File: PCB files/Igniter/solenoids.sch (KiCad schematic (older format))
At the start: 29 parts, among them Q2 N MOSFET, Q4 N MOSFET, U2 FDS8984, U3 FDS8984, U4 FDS8984

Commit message: 12/5/2019
-Updated netlist and board layout with added dsub15 for solenoids
-Fixed all barrel jack connectors
-Removed some 2560 pins for routing
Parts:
- J4: renamed from J?; footprint (none) -> Connector_Dsub:DSUB-15-HD_Female_Horizontal_P2.29x1.98mm_EdgePinOffset3.03mm_Housed_MountingHolesOffset4.94mm
- gave numbers to parts that had none: 9
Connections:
- wire segments 77 -> 78
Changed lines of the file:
@@
 LIBS:interface
 LIBS:Igniter-cache
-EELAYER 29 0
+EELAYER 26 0
 EELAYER END
 $Descr A4 11693 8268
@@
 Connection ~ 8225 3660
 $Comp
-L Connector:Conn_01x11_Female J?
+L Connector:Conn_01x11_Female J4
 U 1 1 5DE8A6FF
 P 6176 2383
-F 0 "J?" V 6341 2363 50  0000 C CNN
+F 0 "J4" V 6341 2363 50  0000 C CNN
 F 1 "SOL_D15" V 6250 2363 50  0000 C CNN
-F 2 "" H 6176 2383 50  0001 C CNN
+F 2 "Connector_Dsub:DSUB-15-HD_Female_Horizontal_P2.29x1.98mm_EdgePinOffset3.03mm_Housed_MountingHolesOffset4.94mm" H 6176 2383 50  0001 C CNN
 F 3 "~" H 6176 2383 50  0001 C CNN
 	1    6176 2383
@@
 SOL1-
 $Comp
-L power:GNDREF #PWR?
+L power:GNDREF #PWR032
 U 1 1 5DF3EB19
 P 5922 2883
-F 0 "#PWR?" H 5922 2633 50  0001 C CNN
+F 0 "#PWR032" H 5922 2633 50  0001 C CNN
 F 1 "GNDREF" H 5927 2710 50  0001 C CNN
 F 2 "" H 5922 2883 50  0001 C CNN
@@
 	3784 2424 3684 2524
 Entry Wire Line
-	3941 4352 3841 4452
+	3783 4000 3683 4100
 Entry Wire Line
-	3957 4699 3857 4799
+	3783 4381 3683 4481
 Wire Wire Line
 	2927 2775 2927 2803
@@
 P 4783 3391
 AR Path="/5DFE00A1" Ref="#PWR?"  Part="1"
-AR Path="/5DB4D508/5DFE00A1" Ref="#PWR?"  Part="1"
-F 0 "#PWR?" H 4783 3141 50  0001 C CNN
+AR Path="/5DB4D508/5DFE00A1" Ref="#PWR030"  Part="1"
+F 0 "#PWR030" H 4783 3141 50  0001 C CNN
 F 1 "GNDREF" H 4788 3218 50  0001 C CNN
 F 2 "" H 4783 3391 50  0001 C CNN
@@
 P 4783 3241
 AR Path="/5DFE00AB" Ref="R?"  Part="1"
-AR Path="/5DB4D508/5DFE00AB" Ref="R?"  Part="1"
-F 0 "R?" V 4703 3191 50  0000 L CNN
+AR Path="/5DB4D508/5DFE00AB" Ref="R3"  Part="1"
+F 0 "R3" V 4703 3191 50  0000 L CNN
 F 1 "10k" V 4783 3171 50  0000 L CNN
 F 2 "Resistor_SMD:R_1206_3216Metric" V 4713 3241 50  0001 C CNN
@@
 $EndComp
 $Comp
-L power:+24V #PWR?
+L power:+24V #PWR019
 U 1 1 5DFE00B5
 P 4443 2307
-F 0 "#PWR?" H 4443 2157 50  0001 C CNN
+F 0 "#PWR019" H 4443 2157 50  0001 C CNN
 F 1 "+24V" H 4458 2480 50  0000 C CNN
 F 2 "" H 4443 2307 50  0001 C CNN
@@
 AR Path="/5D9BEB88/5DFE00C0" Ref="Q?"  Part="1"
 AR Path="/5DFE00C0" Ref="Q?"  Part="1"
-AR Path="/5DB4D508/5DFE00C0" Ref="Q?"  Part="1"
-F 0 "Q?" H 4749 3137 50  0000 L CNN
+AR Path="/5DB4D508/5DFE00C0" Ref="Q5"  Part="1"
+F 0 "Q5" H 4749 3137 50  0000 L CNN
 F 1 "N MOSFET" H 4749 3091 50  0001 L CNN
 F 2 "Package_TO_SOT_SMD:SOT-223" H 4743 3191 50  0001 C CNN
@@
 	4443 3291 4443 3391
 $Comp
-L power:GNDREF #PWR?
+L power:GNDREF #PWR020
 U 1 1 5DFE00CB
 P 4443 3391
-F 0 "#PWR?" H 4443 3141 50  0001 C CNN
+F 0 "#PWR020" H 4443 3141 50  0001 C CNN
 F 1 "GNDREF" H 4448 3218 50  0001 C CNN
 F 2 "" H 4443 3391 50  0001 C CNN
@@
 $EndComp
 $Comp
-L Device:D D?
+L Device:D D5
 U 1 1 5DFE00D5
 P 4443 2626
-F 0 "D?" V 4397 2705 50  0000 L CNN
+F 0 "D5" V 4397 2705 50  0000 L CNN
 F 1 "D" V 4488 2705 50  0000 L CNN
 F 2 "Diode_SMD:D_SOD-123F" H 4443 2626 50  0001 C CNN
@@
 P 2586 4968
 AR Path="/5DFFE41D" Ref="#PWR?"  Part="1"
-AR Path="/5DB4D508/5DFFE41D" Ref="#PWR?"  Part="1"
-F 0 "#PWR?" H 2586 4718 50  0001 C CNN
+AR Path="/5DB4D508/5DFFE41D" Ref="#PWR014"  Part="1"
+F 0 "#PWR014" H 2586 4718 50  0001 C CNN
 F 1 "GNDREF" H 2591 4795 50  0001 C CNN
 F 2 "" H 2586 4968 50  0001 C CNN
@@
 P 2586 4818
 AR Path="/5DFFE427" Ref="R?"  Part="1"
-AR Path="/5DB4D508/5DFFE427" Ref="R?"  Part="1"
-F 0 "R?" V 2506 4768 50  0000 L CNN
+AR Path="/5DB4D508/5DFFE427" Ref="R2"  Part="1"
+F 0 "R2" V 2506 4768 50  0000 L CNN
 F 1 "10k" V 2586 4748 50  0000 L CNN
 F 2 "Resistor_SMD:R_1206_3216Metric" V 2516 4818 50  0001 C CNN
@@
 $EndComp
 $Comp
-L power:+24V #PWR?
+L power:+24V #PWR015
 U 1 1 5DFFE431
 P 2926 3884
-F 0 "#PWR?" H 2926 3734 50  0001 C CNN
+F 0 "#PWR015" H 2926 3734 50  0001 C CNN
 F 1 "+24V" H 2941 4057 50  0000 C CNN
 F 2 "" H 2926 3884 50  0001 C CNN
@@
 AR Path="/5D9BEB88/5DFFE43C" Ref="Q?"  Part="1"
 AR Path="/5DFFE43C" Ref="Q?"  Part="1"
-AR Path="/5DB4D508/5DFFE43C" Ref="Q?"  Part="1"
-F 0 "Q?" H 3032 4714 50  0000 L CNN
+AR Path="/5DB4D508/5DFFE43C" Ref="Q3"  Part="1"
+F 0 "Q3" H 3032 4714 50  0000 L CNN
 F 1 "N MOSFET" H 3032 4668 50  0001 L CNN
 F 2 "Package_TO_SOT_SMD:SOT-223" H 3026 4768 50  0001 C CNN
@@
 	2926 4868 2926 4968
 $Comp
-L power:GNDREF #PWR?
+L power:GNDREF #PWR016
 U 1 1 5DFFE447
 P 2926 4968
-F 0 "#PWR?" H 2926 4718 50  0001 C CNN
+F 0 "#PWR016" H 2926 4718 50  0001 C CNN
 F 1 "GNDREF" H 2931 4795 50  0001 C CNN
 F 2 "" H 2926 4968 50  0001 C CNN
@@
 $EndComp
 $Comp
-L Device:D D?
+L Device:D D3
 U 1 1 5DFFE451
 P 2926 4203
-F 0 "D?" V 2880 4282 50  0000 L CNN
+F 0 "D3" V 2880 4282 50  0000 L CNN
 F 1 "D" V 2971 4282 50  0000 L CNN
 F 2 "Diode_SMD:D_SOD-123F" H 2926 4203 50  0001 C CNN
@@
 P 5029 4966
 AR Path="/5E011B64" Ref="#PWR?"  Part="1"
-AR Path="/5DB4D508/5E011B64" Ref="#PWR?"  Part="1"
-F 0 "#PWR?" H 5029 4716 50  0001 C CNN
+AR Path="/5DB4D508/5E011B64" Ref="#PWR031"  Part="1"
+F 0 "#PWR031" H 5029 4716 50  0001 C CNN
 F 1 "GNDREF" H 5034 4793 50  0001 C CNN
 F 2 "" H 5029 4966 50  0001 C CNN
@@
 P 5029 4816
 AR Path="/5E011B6E" Ref="R?"  Part="1"
-AR Path="/5DB4D508/5E011B6E" Ref="R?"  Part="1"
-F 0 "R?" V 4949 4766 50  0000 L CNN
+AR Path="/5DB4D508/5E011B6E" Ref="R11"  Part="1"
+F 0 "R11" V 4949 4766 50  0000 L CNN
 F 1 "10k" V 5029 4746 50  0000 L CNN
 F 2 "Resistor_SMD:R_1206_3216Metric" V 4959 4816 50  0001 C CNN
@@
 $EndComp
 $Comp
-L power:+24V #PWR?
+L power:+24V #PWR023
 U 1 1 5E011B78
 P 4689 3882
-F 0 "#PWR?" H 4689 3732 50  0001 C CNN
+F 0 "#PWR023" H 4689 3732 50  0001 C CNN
 F 1 "+24V" H 4704 4055 50  0000 C CNN
 F 2 "" H 4689 3882 50  0001 C CNN
@@
 AR Path="/5D9BEB88/5E011B83" Ref="Q?"  Part="1"
 AR Path="/5E011B83" Ref="Q?"  Part="1"
-AR Path="/5DB4D508/5E011B83" Ref="Q?"  Part="1"
-F 0 "Q?" H 4995 4712 50  0000 L CNN
+AR Path="/5DB4D508/5E011B83" Ref="Q6"  Part="1"
+F 0 "Q6" H 4995 4712 50  0000 L CNN
 F 1 "N MOSFET" H 4995 4666 50  0001 L CNN
 F 2 "Package_TO_SOT_SMD:SOT-223" H 4989 4766 50  0001 C CNN
@@
 	4689 4866 4689 4966
 $Comp
-L power:GNDREF #PWR?
+L power:GNDREF #PWR027
 U 1 1 5E011B8E
 P 4689 4966
-F 0 "#PWR?" H 4689 4716 50  0001 C CNN
+F 0 "#PWR027" H 4689 4716 50  0001 C CNN
 F 1 "GNDREF" H 4694 4793 50  0001 C CNN
 F 2 "" H 4689 4966 50  0001 C CNN
@@
 $EndComp
 $Comp
-L Device:D D?
+L Device:D D6
 U 1 1 5E011B98
 P 4689 4201
-F 0 "D?" V 4643 4280 50  0000 L CNN
+F 0 "D6" V 4643 4280 50  0000 L CNN
 F 1 "D" V 4734 4280 50  0000 L CNN
 F 2 "Diode_SMD:D_SOD-123F" H 4689 4201 50  0001 C CNN
@@
 Wire Wire Line
 	4689 3882 4689 4000
-Wire Wire Line
-	4032 4000 4689 4000
 Connection ~ 4689 4000
 Wire Wire Line
@@
 Wire Wire Line
 	4689 4351 4689 4379
-Wire Wire Line
-	4032 4379 4689 4379
 Connection ~ 4689 4379
 Wire Wire Line
@@
 Wire Bus Line
 	4831 1965 5683 1965
+Wire Wire Line
+	3783 4379 3783 4381
+Wire Wire Line
+	3783 4379 4689 4379
+Wire Wire Line
+	3783 4000 4689 4000
 Wire Bus Line
 	3684 1965 3684 6227

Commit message: 12/9/2019
Schematic
-Removed SOL bus connector, changed to individual circuits
-Removed pressure transducer shared connector. changed back to individual circuits
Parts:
- removed J4: SOL_D15, Connector_Dsub:DSUB-15-HD_Female_Horizontal_P2.29x1.98mm_EdgePinOffset3.03mm_Housed_MountingHolesOffset4.94mm, symbol Connector:Conn_01x11_Female
- removed R18: 10k, Resistor_SMD:R_1206_3216Metric, symbol Device:R
- added J10: SL2, Connector_Molex:Molex_Nano-Fit_105309-xx03_1x03_P2.50mm_Vertical, symbol Connector:Conn_01x03_Female
- added J11: SL3, Connector_Molex:Molex_Nano-Fit_105309-xx03_1x03_P2.50mm_Vertical, symbol Connector:Conn_01x03_Female
- added J12: SL4, Connector_Molex:Molex_Nano-Fit_105309-xx03_1x03_P2.50mm_Vertical, symbol Connector:Conn_01x03_Female
- added J13: SL5, Connector_Molex:Molex_Nano-Fit_105309-xx03_1x03_P2.50mm_Vertical, symbol Connector:Conn_01x03_Female
- added J9: SL1, Connector_Molex:Molex_Nano-Fit_105309-xx03_1x03_P2.50mm_Vertical, symbol Connector:Conn_01x03_Female
- added R12: 10k, Resistor_SMD:R_1206_3216Metric, symbol Device:R
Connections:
- net labels removed: SOL1+, SOL1-, SOL2+, SOL2-, SOL3+, SOL3-, SOL4+, SOL4-, SOL5+, SOL5-
- wire segments 78 -> 86
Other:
- note removed: "If these are fail open, we need an emergency stop\nbutton on the board aside from just using the 24V \npower switch as a stop switch"
- moved on the sheet: D2, Q2, R15

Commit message: 12/10/2019
-Selected battery molex connector footprint
-Read netlist
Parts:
- renumbered J11 to J10, J12 to J11, J13 to J12, J9 to J8, J10 to J9
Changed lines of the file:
@@
 	2477 2282 2477 2395
 $Comp
-L Connector:Conn_01x03_Female J9
+L Connector:Conn_01x03_Female J8
 U 1 1 5DF28FFB
 P 1898 2622
-F 0 "J9" H 1790 2297 50  0000 C CNN
+F 0 "J8" H 1790 2297 50  0000 C CNN
 F 1 "SL1" H 1790 2388 50  0000 C CNN
 F 2 "Connector_Molex:Molex_Nano-Fit_105309-xx03_1x03_P2.50mm_Vertical" H 1898 2622 50  0001 C CNN
@@
 	3730 2306 3730 2419
 $Comp
-L Connector:Conn_01x03_Female J10
+L Connector:Conn_01x03_Female J9
 U 1 1 5DF5A5C1
 P 3151 2646
-F 0 "J10" H 3043 2321 50  0000 C CNN
+F 0 "J9" H 3043 2321 50  0000 C CNN
 F 1 "SL2" H 3043 2412 50  0000 C CNN
 F 2 "Connector_Molex:Molex_Nano-Fit_105309-xx03_1x03_P2.50mm_Vertical" H 3151 2646 50  0001 C CNN
@@
 	4967 2330 4967 2443
 $Comp
-L Connector:Conn_01x03_Female J11
+L Connector:Conn_01x03_Female J10
 U 1 1 5DF5F5EE
 P 4388 2670
-F 0 "J11" H 4280 2345 50  0000 C CNN
+F 0 "J10" H 4280 2345 50  0000 C CNN
 F 1 "SL3" H 4280 2436 50  0000 C CNN
 F 2 "Connector_Molex:Molex_Nano-Fit_105309-xx03_1x03_P2.50mm_Vertical" H 4388 2670 50  0001 C CNN
@@
 	2541 4113 2541 4226
 $Comp
-L Connector:Conn_01x03_Female J12
+L Connector:Conn_01x03_Female J11
 U 1 1 5DF79BA0
 P 1962 4453
-F 0 "J12" H 1854 4128 50  0000 C CNN
+F 0 "J11" H 1854 4128 50  0000 C CNN
 F 1 "SL4" H 1854 4219 50  0000 C CNN
 F 2 "Connector_Molex:Molex_Nano-Fit_105309-xx03_1x03_P2.50mm_Vertical" H 1962 4453 50  0001 C CNN
@@
 	3794 4137 3794 4250
 $Comp
-L Connector:Conn_01x03_Female J13
+L Connector:Conn_01x03_Female J12
 U 1 1 5DF79C01
 P 3215 4477
-F 0 "J13" H 3107 4152 50  0000 C CNN
+F 0 "J12" H 3107 4152 50  0000 C CNN
 F 1 "SL5" H 3107 4243 50  0000 C CNN
 F 2 "Connector_Molex:Molex_Nano-Fit_105309-xx03_1x03_P2.50mm_Vertical" H 3215 4477 50  0001 C CNN

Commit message: 12/18/2019
-Changed Solenoid connector to SPOX
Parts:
- J10, J11, J12, J8, J9: footprint Connector_Molex:Molex_Nano-Fit_105309-xx03_1x03_P2.50mm_Vertical -> Connector_Molex:Molex_SPOX_5267-03A_1x03_P2.50mm_Vertical
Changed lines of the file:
@@
 F 0 "J8" H 1790 2297 50  0000 C CNN
 F 1 "SL1" H 1790 2388 50  0000 C CNN
-F 2 "Connector_Molex:Molex_Nano-Fit_105309-xx03_1x03_P2.50mm_Vertical" H 1898 2622 50  0001 C CNN
+F 2 "Connector_Molex:Molex_SPOX_5267-03A_1x03_P2.50mm_Vertical" H 1898 2622 50  0001 C CNN
 F 3 "~" H 1898 2622 50  0001 C CNN
 	1    1898 2622
@@
 F 0 "J9" H 3043 2321 50  0000 C CNN
 F 1 "SL2" H 3043 2412 50  0000 C CNN
-F 2 "Connector_Molex:Molex_Nano-Fit_105309-xx03_1x03_P2.50mm_Vertical" H 3151 2646 50  0001 C CNN
+F 2 "Connector_Molex:Molex_SPOX_5267-03A_1x03_P2.50mm_Vertical" H 3151 2646 50  0001 C CNN
 F 3 "~" H 3151 2646 50  0001 C CNN
 	1    3151 2646
@@
 F 0 "J10" H 4280 2345 50  0000 C CNN
 F 1 "SL3" H 4280 2436 50  0000 C CNN
-F 2 "Connector_Molex:Molex_Nano-Fit_105309-xx03_1x03_P2.50mm_Vertical" H 4388 2670 50  0001 C CNN
+F 2 "Connector_Molex:Molex_SPOX_5267-03A_1x03_P2.50mm_Vertical" H 4388 2670 50  0001 C CNN
 F 3 "~" H 4388 2670 50  0001 C CNN
 	1    4388 2670
@@
 F 0 "J11" H 1854 4128 50  0000 C CNN
 F 1 "SL4" H 1854 4219 50  0000 C CNN
-F 2 "Connector_Molex:Molex_Nano-Fit_105309-xx03_1x03_P2.50mm_Vertical" H 1962 4453 50  0001 C CNN
+F 2 "Connector_Molex:Molex_SPOX_5267-03A_1x03_P2.50mm_Vertical" H 1962 4453 50  0001 C CNN
 F 3 "~" H 1962 4453 50  0001 C CNN
 	1    1962 4453
@@
 F 0 "J12" H 3107 4152 50  0000 C CNN
 F 1 "SL5" H 3107 4243 50  0000 C CNN
-F 2 "Connector_Molex:Molex_Nano-Fit_105309-xx03_1x03_P2.50mm_Vertical" H 3215 4477 50  0001 C CNN
+F 2 "Connector_Molex:Molex_SPOX_5267-03A_1x03_P2.50mm_Vertical" H 3215 4477 50  0001 C CNN
 F 3 "~" H 3215 4477 50  0001 C CNN
 	1    3215 4477

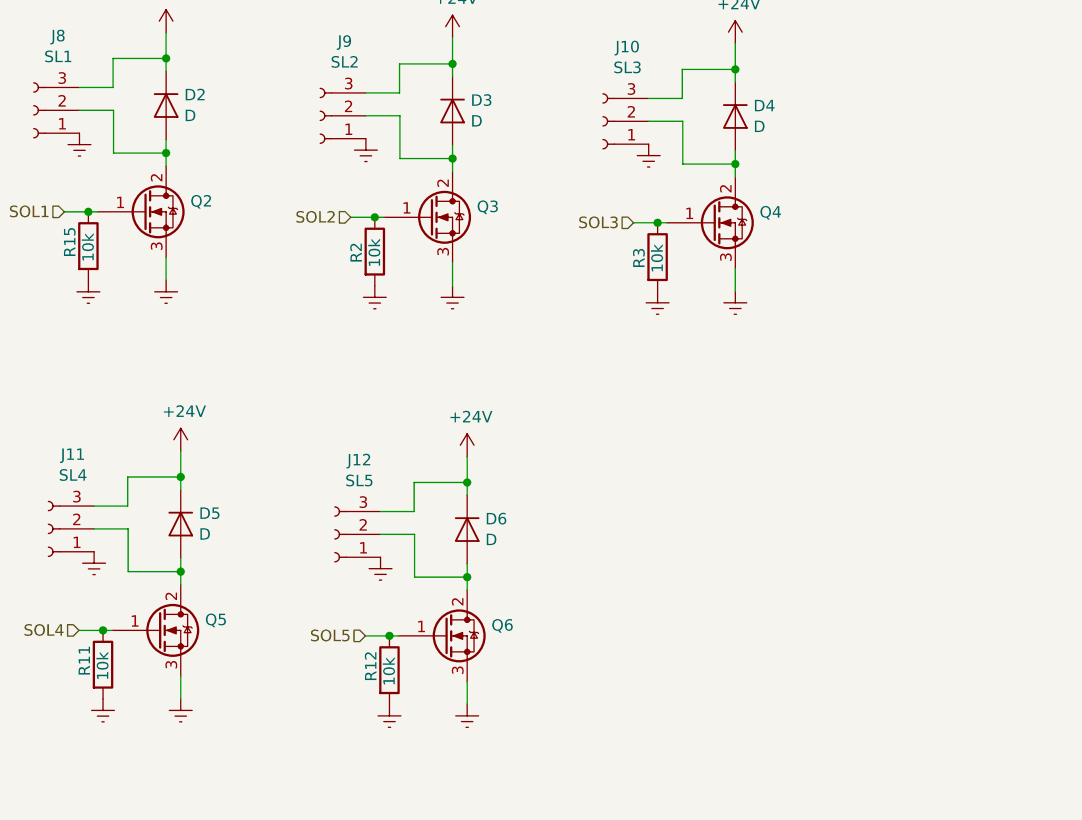
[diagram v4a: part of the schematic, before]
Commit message: 1/9/2019
-Set design rules to match with jlcpcb
-Began laying out power and some signal traces
-Changed FET symbol to 4pin to match sot223 footprint
Removed unused Arduino pins: (5V3,5V4,D22-D39)
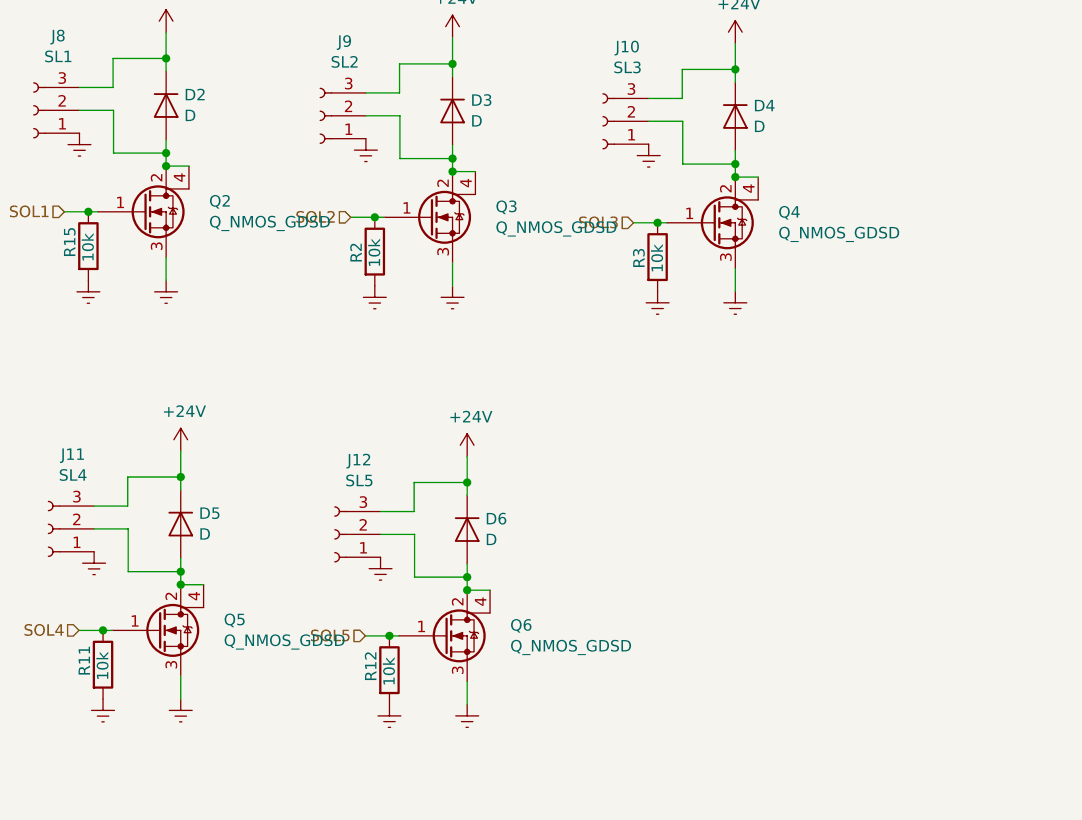
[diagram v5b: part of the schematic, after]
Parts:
- removed Q2, Q3, Q4, Q5, Q6: N MOSFET, Package_TO_SOT_SMD:SOT-223, symbol Device:Q_NMOS_GDS
- added Q2, Q3, Q4, Q5, Q6: Q_NMOS_GDSD, Package_TO_SOT_SMD:SOT-223, symbol Device:Q_NMOS_GDSD
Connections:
- net GNDREF: now also Q2.3 (S), Q3.3 (S), Q4.3 (S), Q5.3 (S), Q6.3 (S)
- net SOL1: now also Q2.1 (G)
- net SOL2: now also Q3.1 (G)
- net SOL3: now also Q4.1 (G)
- net SOL4: now also Q5.1 (G)
- net SOL5: now also Q6.1 (G)
- net at D2.2 (A), J8.2 (Pin_2): now also Q2.2 (D), Q2.4 (D)
- net at D3.2 (A), J9.2 (Pin_2): now also Q3.2 (D), Q3.4 (D)
- net at D4.2 (A), J10.2 (Pin_2): now also Q4.2 (D), Q4.4 (D)
- net at D5.2 (A), J11.2 (Pin_2): now also Q5.2 (D), Q5.4 (D)
- net at D6.2 (A), J12.2 (Pin_2): now also Q6.2 (D), Q6.4 (D)
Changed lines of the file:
@@
 Text HLabel 2032 3066 0    50   Input ~ 0
 SOL1
-$Comp
-L Device:Q_NMOS_GDS Q?
-U 1 1 5DB4DFB4
-P 2377 3066
-AR Path="/5D9BEB88/5DB4DFB4" Ref="Q?"  Part="1"
-AR Path="/5DB4DFB4" Ref="Q?"  Part="1"
-AR Path="/5DB4D508/5DB4DFB4" Ref="Q2"  Part="1"
-F 0 "Q2" H 2583 3112 50  0000 L CNN
-F 1 "N MOSFET" H 2583 3066 50  0001 L CNN
-F 2 "Package_TO_SOT_SMD:SOT-223" H 2577 3166 50  0001 C CNN
-F 3 "~" H 2377 3066 50  0001 C CNN
-	1    2377 3066
-	1    0    0    -1
-$EndComp
 Wire Wire Line
 	2477 3266 2477 3366
@@
 Text HLabel 3285 3090 0    50   Input ~ 0
 SOL2
-$Comp
-L Device:Q_NMOS_GDS Q?
-U 1 1 5DF5A597
-P 3630 3090
-AR Path="/5D9BEB88/5DF5A597" Ref="Q?"  Part="1"
-AR Path="/5DF5A597" Ref="Q?"  Part="1"
-AR Path="/5DB4D508/5DF5A597" Ref="Q3"  Part="1"
-F 0 "Q3" H 3836 3136 50  0000 L CNN
-F 1 "N MOSFET" H 3836 3090 50  0001 L CNN
-F 2 "Package_TO_SOT_SMD:SOT-223" H 3830 3190 50  0001 C CNN
-F 3 "~" H 3630 3090 50  0001 C CNN
-	1    3630 3090
-	1    0    0    -1
-$EndComp
 Wire Wire Line
 	3730 3290 3730 3390
@@
 Text HLabel 4522 3114 0    50   Input ~ 0
 SOL3
-$Comp
-L Device:Q_NMOS_GDS Q?
-U 1 1 5DF5F5C4
-P 4867 3114
-AR Path="/5D9BEB88/5DF5F5C4" Ref="Q?"  Part="1"
-AR Path="/5DF5F5C4" Ref="Q?"  Part="1"
-AR Path="/5DB4D508/5DF5F5C4" Ref="Q4"  Part="1"
-F 0 "Q4" H 5073 3160 50  0000 L CNN
-F 1 "N MOSFET" H 5073 3114 50  0001 L CNN
-F 2 "Package_TO_SOT_SMD:SOT-223" H 5067 3214 50  0001 C CNN
-F 3 "~" H 4867 3114 50  0001 C CNN
-	1    4867 3114
-	1    0    0    -1
-$EndComp
 Wire Wire Line
 	4967 3314 4967 3414
@@
 Text HLabel 2096 4897 0    50   Input ~ 0
 SOL4
-$Comp
-L Device:Q_NMOS_GDS Q?
-U 1 1 5DF79B76
-P 2441 4897
-AR Path="/5D9BEB88/5DF79B76" Ref="Q?"  Part="1"
-AR Path="/5DF79B76" Ref="Q?"  Part="1"
-AR Path="/5DB4D508/5DF79B76" Ref="Q5"  Part="1"
-F 0 "Q5" H 2647 4943 50  0000 L CNN
-F 1 "N MOSFET" H 2647 4897 50  0001 L CNN
-F 2 "Package_TO_SOT_SMD:SOT-223" H 2641 4997 50  0001 C CNN
-F 3 "~" H 2441 4897 50  0001 C CNN
-	1    2441 4897
-	1    0    0    -1
-$EndComp
 Wire Wire Line
 	2541 5097 2541 5197
@@
 Text HLabel 3349 4921 0    50   Input ~ 0
 SOL5
-$Comp
-L Device:Q_NMOS_GDS Q?
-U 1 1 5DF79BD7
-P 3694 4921
-AR Path="/5D9BEB88/5DF79BD7" Ref="Q?"  Part="1"
-AR Path="/5DF79BD7" Ref="Q?"  Part="1"
-AR Path="/5DB4D508/5DF79BD7" Ref="Q6"  Part="1"
-F 0 "Q6" H 3900 4967 50  0000 L CNN
-F 1 "N MOSFET" H 3900 4921 50  0001 L CNN
-F 2 "Package_TO_SOT_SMD:SOT-223" H 3894 5021 50  0001 C CNN
-F 3 "~" H 3694 4921 50  0001 C CNN
-	1    3694 4921
-	1    0    0    -1
-$EndComp
 Wire Wire Line
 	3794 5121 3794 5221
@@
 Wire Wire Line
 	3794 4250 3794 4306
+$Comp
+L Device:Q_NMOS_GDSD Q2
+U 1 1 5E188C29
+P 2377 3066
+F 0 "Q2" H 2665 3112 50  0000 L CNN
+F 1 "Q_NMOS_GDSD" H 2665 3021 50  0000 L CNN
+F 2 "Package_TO_SOT_SMD:SOT-223" H 2577 3166 50  0001 C CNN
+F 3 "~" H 2377 3066 50  0001 C CNN
+	1    2377 3066
+	1    0    0    -1
+$EndComp
+Wire Wire Line
+	2577 2866 2477 2866
+Connection ~ 2477 2866
+$Comp
+L Device:Q_NMOS_GDSD Q3
+U 1 1 5E193C58
+P 3630 3090
+F 0 "Q3" H 3918 3136 50  0000 L CNN
+F 1 "Q_NMOS_GDSD" H 3918 3045 50  0000 L CNN
+F 2 "Package_TO_SOT_SMD:SOT-223" H 3830 3190 50  0001 C CNN
+F 3 "~" H 3630 3090 50  0001 C CNN
+	1    3630 3090
+	1    0    0    -1
+$EndComp
+$Comp
+L Device:Q_NMOS_GDSD Q4
+U 1 1 5E19577C
+P 4867 3114
+F 0 "Q4" H 5155 3160 50  0000 L CNN
+F 1 "Q_NMOS_GDSD" H 5155 3069 50  0000 L CNN
+F 2 "Package_TO_SOT_SMD:SOT-223" H 5067 3214 50  0001 C CNN
+F 3 "~" H 4867 3114 50  0001 C CNN
+	1    4867 3114
+	1    0    0    -1
+$EndComp
+$Comp
+L Device:Q_NMOS_GDSD Q5
+U 1 1 5E197D50
+P 2441 4897
+F 0 "Q5" H 2729 4943 50  0000 L CNN
+F 1 "Q_NMOS_GDSD" H 2729 4852 50  0000 L CNN
+F 2 "Package_TO_SOT_SMD:SOT-223" H 2641 4997 50  0001 C CNN
+F 3 "~" H 2441 4897 50  0001 C CNN
+	1    2441 4897
+	1    0    0    -1
+$EndComp
+$Comp
+L Device:Q_NMOS_GDSD Q6
+U 1 1 5E19A09A
+P 3694 4921
+F 0 "Q6" H 3982 4967 50  0000 L CNN
+F 1 "Q_NMOS_GDSD" H 3982 4876 50  0000 L CNN
+F 2 "Package_TO_SOT_SMD:SOT-223" H 3894 5021 50  0001 C CNN
+F 3 "~" H 3694 4921 50  0001 C CNN
+	1    3694 4921
+	1    0    0    -1
+$EndComp
+Wire Wire Line
+	2641 4697 2541 4697
+Connection ~ 2541 4697
+Wire Wire Line
+	3794 4721 3894 4721
+Connection ~ 3794 4721
+Wire Wire Line
+	3830 2890 3730 2890
+Connection ~ 3730 2890
+Wire Wire Line
+	5067 2914 4967 2914
+Connection ~ 4967 2914
 $EndSCHEMATC
